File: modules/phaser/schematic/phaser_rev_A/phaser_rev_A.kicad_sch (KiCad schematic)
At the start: 15 parts, among them Q1 2N2978, Q2 2N2978, Q3 2N2978, Q4 2N2978, Q5 2N2978

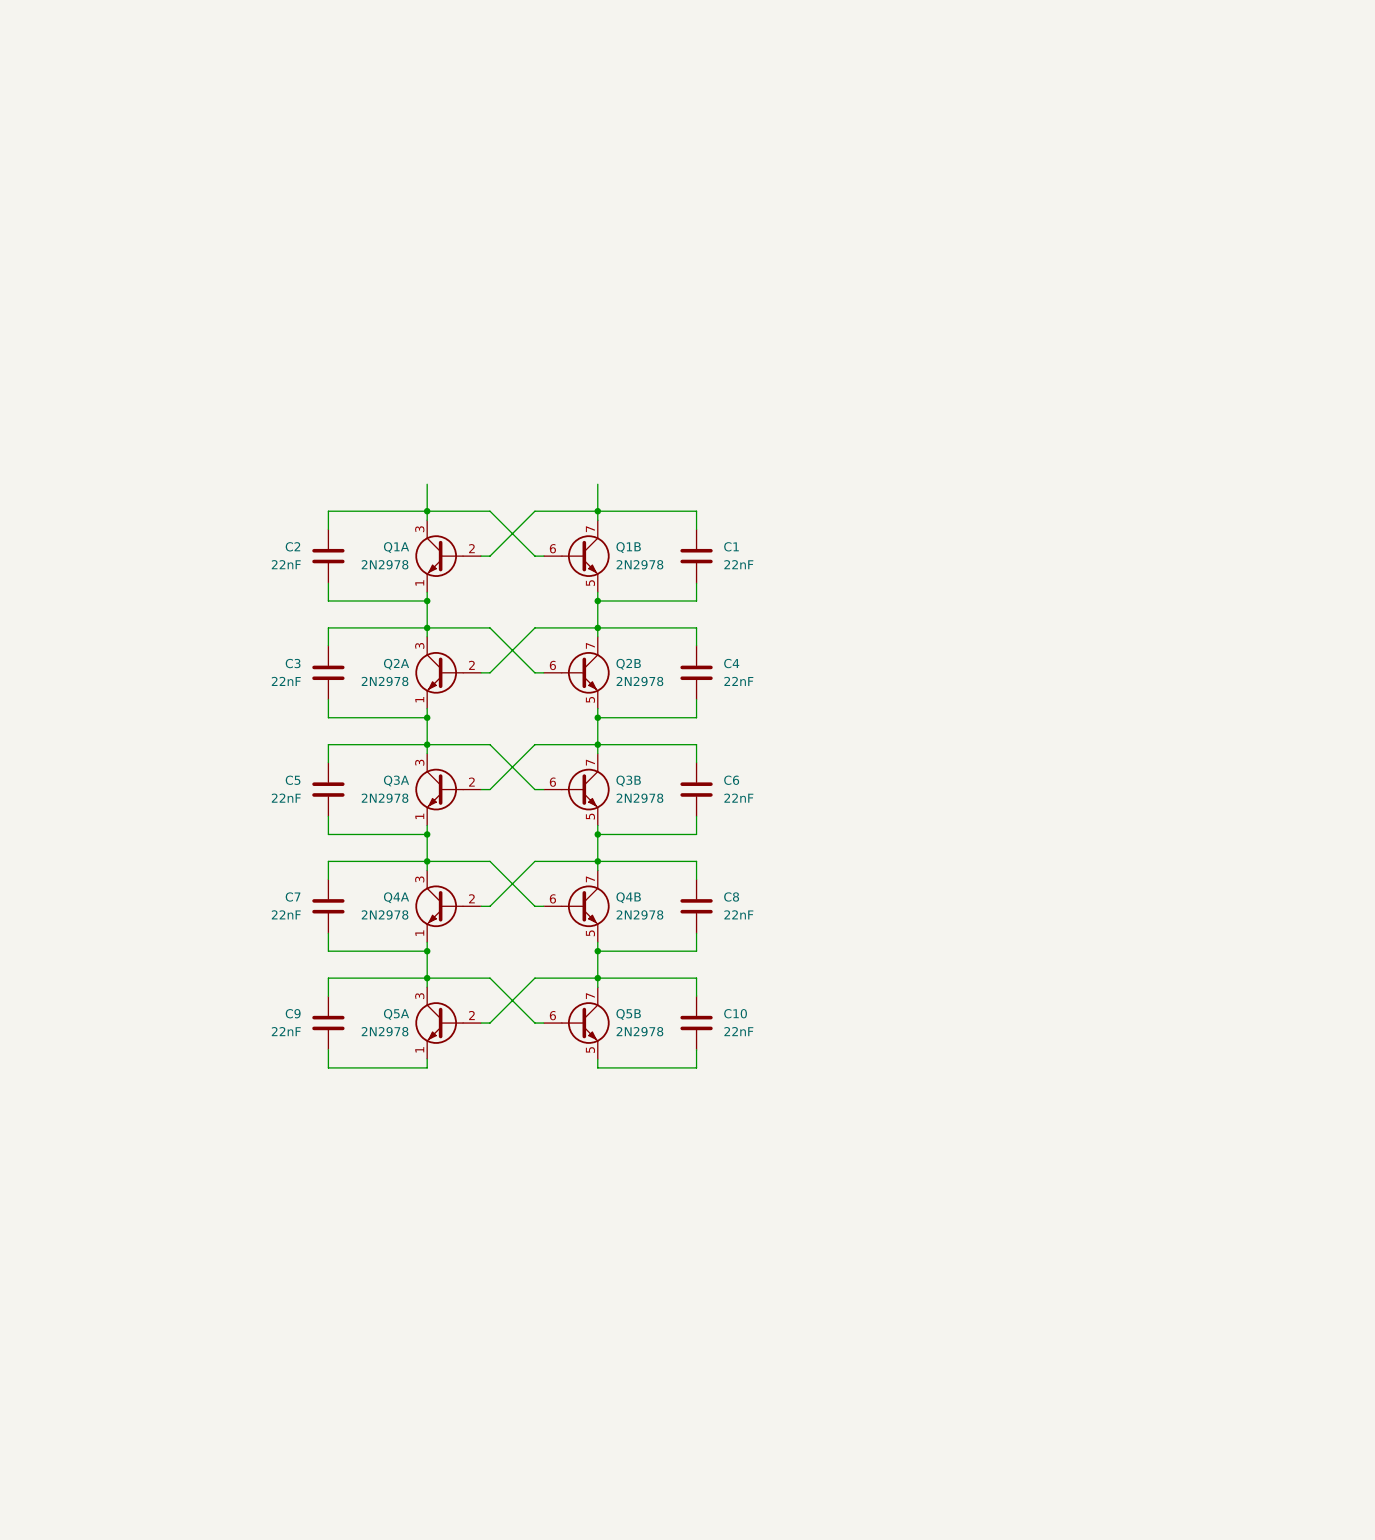
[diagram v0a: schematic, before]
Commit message: first routing of the PCB added a case study for the phaser
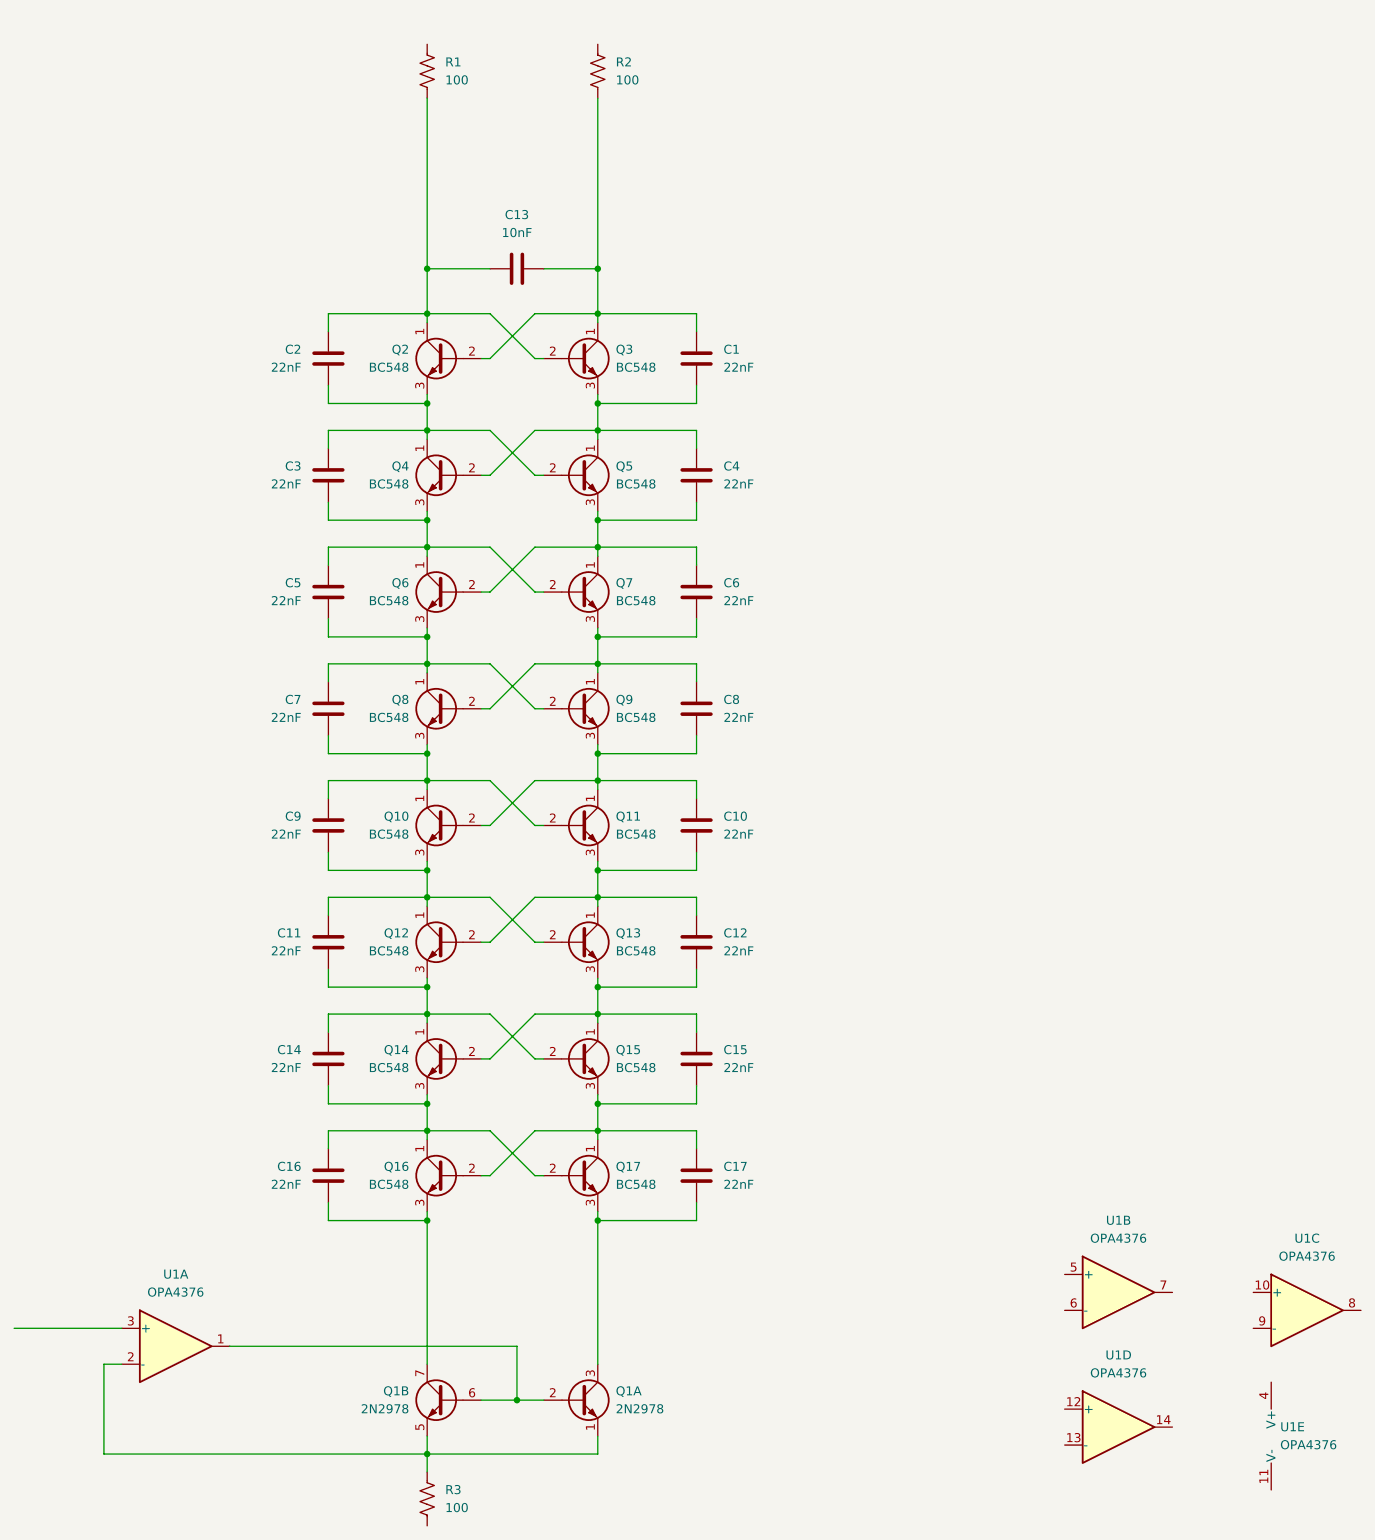
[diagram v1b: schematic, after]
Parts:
- removed Q2, Q3, Q4, Q5: 2N2978, ProjectLib_Transient:TO-5-6, symbol ProjectLib_Transient:2N2978
- added C11, C12, C14, C15, C16, C17: 22nF, Capacitor_THT:C_Rect_L7.0mm_W2.0mm_P5.00mm, symbol Device:C
- added C13: 10nF, Capacitor_THT:C_Rect_L7.0mm_W2.0mm_P5.00mm, symbol Device:C
- added Q10, Q11, Q12, Q13, Q14, Q15, Q16, Q17, Q2, Q3, Q4, Q5, Q6, Q7, Q8, Q9: BC548, Package_TO_SOT_THT:TO-92L_Inline_Wide, symbol Transistor_BJT:BC548
- added R1, R2, R3: 100, Resistor_THT:R_Axial_DIN0207_L6.3mm_D2.5mm_P10.16mm_Horizontal, symbol Device:R_US
- added U1: OPA4376, Package_DIP:DIP-14_W7.62mm_LongPads, symbol Amplifier_Operational:OPA4376
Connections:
- net at C9.2: now also C11.1, Q10.3 (E), Q12.1 (C), Q13.2 (B)
- net at C10.1, C8.2: now also Q10.2 (B), Q11.1 (C), Q9.3 (E)
- net at C7.2, C9.1: now also Q10.1 (C), Q11.2 (B), Q8.3 (E)
- net at C5.2, C7.1: now also Q6.3 (E), Q8.1 (C), Q9.2 (B)
- net at C6.2, C8.1: now also Q7.3 (E), Q8.2 (B), Q9.1 (C)
- net at C2.2, C3.1: now also Q2.3 (E), Q4.1 (C), Q5.2 (B); no longer Q1.1 (E1)
- net at C3.2, C5.1: now also Q4.3 (E), Q6.1 (C), Q7.2 (B)
- net at C1.2, C4.1: now also Q3.3 (E), Q4.2 (B), Q5.1 (C); no longer Q1.5 (E2)
- net at C10.2: now also C12.1, Q11.3 (E), Q12.2 (B), Q13.1 (C)
- net at C4.2, C6.1: now also Q5.3 (E), Q6.2 (B), Q7.1 (C)
- new net: C1.1, C13.2, Q2.2 (B), Q3.1 (C), R2.2
- new net: C13.1, C2.1, Q2.1 (C), Q3.2 (B), R1.2
- new net: C12.2, C15.1, Q13.3 (E), Q14.2 (B), Q15.1 (C)
- new net: C11.2, C14.1, Q12.3 (E), Q14.1 (C), Q15.2 (B)
- new net: C15.2, C17.1, Q15.3 (E), Q16.2 (B), Q17.1 (C)
- new net: C14.2, C16.1, Q14.3 (E), Q16.1 (C), Q17.2 (B)
- new net: C17.2, Q1.3 (C1), Q17.3 (E)
- new net: Q1.2 (B1), Q1.6 (B2), U1.1
- new net: Q1.1 (E1), Q1.5 (E2), R3.1, U1.2 (-)
- new net: C16.2, Q1.7 (C2), Q16.3 (E)
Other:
- moved on the sheet: C1, C10, C2, C3, C4, C5, C6, C7, C8, C9

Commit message: updated pcb layout
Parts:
- added C18, C19: 33µF, Capacitor_THT:CP_Radial_D8.0mm_P3.80mm, symbol Device:C_Polarized
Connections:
- net at C1.1, C13.2, Q2.2 (B)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: now also C18.1
- net at C13.1, C2.1, Q2.1 (C)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: now also C19.1
- net at R2.1: now also R1.1
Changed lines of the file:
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@@
 	)
 	(junction
+		(at 120.65 62.23)
+		(diameter 0)
+		(color 0 0 0 0)
+	)
+	(junction
 		(at 120.65 179.07)
 		(diameter 0)
@@
 	)
 	(junction
+		(at 144.78 38.1)
+		(diameter 0)
+		(color 0 0 0 0)
+	)
+	(junction
 		(at 120.65 158.75)
 		(diameter 0)
@@
 	)
 	(junction
+		(at 144.78 54.61)
+		(diameter 0)
+		(color 0 0 0 0)
+	)
+	(junction
 		(at 120.65 80.01)
 		(diameter 0)
@@
 	(wire
 		(pts
+			(xy 120.65 41.91) (xy 120.65 38.1)
+		)
+		(stroke
+			(width 0)
+			(type default)
+		)
+	)
+	(wire
+		(pts
 			(xy 120.65 195.58) (xy 120.65 196.85)
 		)
@@
 	(wire
 		(pts
+			(xy 144.78 54.61) (xy 144.78 73.66)
+		)
+		(stroke
+			(width 0)
+			(type default)
+		)
+	)
+	(wire
+		(pts
 			(xy 120.65 73.66) (xy 129.54 73.66)
 		)
@@
 	(wire
 		(pts
+			(xy 168.91 62.23) (xy 177.8 62.23)
+		)
+		(stroke
+			(width 0)
+			(type default)
+		)
+	)
+	(wire
+		(pts
 			(xy 120.65 80.01) (xy 129.54 80.01)
 		)
@@
 	(wire
 		(pts
+			(xy 120.65 62.23) (xy 120.65 73.66)
+		)
+		(stroke
+			(width 0)
+			(type default)
+		)
+	)
+	(wire
+		(pts
 			(xy 135.89 152.4) (xy 129.54 146.05)
 		)
@@
 	(wire
 		(pts
+			(xy 144.78 38.1) (xy 144.78 41.91)
+		)
+		(stroke
+			(width 0)
+			(type default)
+		)
+	)
+	(wire
+		(pts
 			(xy 158.75 82.55) (xy 158.75 80.01)
 		)
@@
 	(wire
 		(pts
+			(xy 120.65 62.23) (xy 161.29 62.23)
+		)
+		(stroke
+			(width 0)
+			(type default)
+		)
+	)
+	(wire
+		(pts
 			(xy 135.89 168.91) (xy 129.54 162.56)
 		)
@@
 	(wire
 		(pts
-			(xy 120.65 49.53) (xy 120.65 73.66)
+			(xy 120.65 49.53) (xy 120.65 62.23)
 		)
 		(stroke
@@
 	(wire
 		(pts
+			(xy 168.91 54.61) (xy 177.8 54.61)
+		)
+		(stroke
+			(width 0)
+			(type default)
+		)
+	)
+	(wire
+		(pts
 			(xy 144.78 173.99) (xy 144.78 175.26)
 		)
@@
 	(wire
 		(pts
-			(xy 144.78 49.53) (xy 144.78 73.66)
+			(xy 144.78 49.53) (xy 144.78 54.61)
 		)
 		(stroke
@@
 	(wire
 		(pts
+			(xy 144.78 54.61) (xy 161.29 54.61)
+		)
+		(stroke
+			(width 0)
+			(type default)
+		)
+	)
+	(wire
+		(pts
 			(xy 144.78 109.22) (xy 144.78 113.03)
 		)
@@
 	(wire
 		(pts
+			(xy 144.78 38.1) (xy 167.64 38.1)
+		)
+		(stroke
+			(width 0)
+			(type default)
+		)
+	)
+	(wire
+		(pts
+			(xy 120.65 38.1) (xy 144.78 38.1)
+		)
+		(stroke
+			(width 0)
+			(type default)
+		)
+	)
+	(wire
+		(pts
 			(xy 144.78 125.73) (xy 144.78 129.54)
 		)
@@
 	)
 	(symbol
+		(lib_id "Device:C_Polarized")
+		(at 165.1 54.61 90)
+		(unit 1)
+		(exclude_from_sim no)
+		(in_bom yes)
+		(on_board yes)
+		(dnp no)
+		(fields_autoplaced yes)
+		(property "Reference" "C18"
+			(at 164.211 46.99 90)
+			(effects
+				(font
+					(size 1.27 1.27)
+				)
+			)
+		)
+		(property "Value" "33µF"
+			(at 164.211 49.53 90)
+			(effects
+				(font
+					(size 1.27 1.27)
+				)
+			)
+		)
+		(property "Footprint" "Capacitor_THT:CP_Radial_D8.0mm_P3.80mm"
+			(at 168.91 53.6448 0)
+			(effects
+				(font
+					(size 1.27 1.27)
+				)
+				(hide yes)
+			)
+		)
+		(property "Datasheet" "~"
+			(at 165.1 54.61 0)
+			(effects
+				(font
+					(size 1.27 1.27)
+				)
+				(hide yes)
+			)
+		)
+		(property "Description" "Polarized capacitor"
+			(at 165.1 54.61 0)
+			(effects
+				(font
+					(size 1.27 1.27)
+				)
+				(hide yes)
+			)
+		)
+		(pin "2"
+		)
+		(pin "1"
+		)
+		(instances
+			(project ""
+				(path "/197f4a44-5606-4614-9f30-04e68d42fe94"
+					(reference "C18")
+					(unit 1)
+				)
+			)
+		)
+	)
+	(symbol
 		(lib_id "Transistor_BJT:BC548")
 		(at 142.24 135.89 0)
@@
 					(unit 1)
 				)
+			)
+		)
+	)
+	(symbol
+		(lib_id "Device:C_Polarized")
+		(at 165.1 62.23 90)
+		(mirror x)
+		(unit 1)
+		(exclude_from_sim no)
+		(in_bom yes)
+		(on_board yes)
+		(dnp no)
+		(property "Reference" "C19"
+			(at 164.211 69.85 90)
+			(effects
+				(font
+					(size 1.27 1.27)
+				)
+			)
+		)
+		(property "Value" "33µF"
+			(at 164.211 67.31 90)
+			(effects
+				(font
+					(size 1.27 1.27)
+				)
+			)
+		)
+		(property "Footprint" "Capacitor_THT:CP_Radial_D8.0mm_P3.80mm"
+			(at 168.91 63.1952 0)
+			(effects
+				(font
+					(size 1.27 1.27)
+				)
+				(hide yes)
+			)
+		)
+		(property "Datasheet" "~"
+			(at 165.1 62.23 0)
+			(effects
+				(font
+					(size 1.27 1.27)
+				)
+				(hide yes)
+			)
+		)
+		(property "Description" "Polarized capacitor"
+			(at 165.1 62.23 0)
+			(effects
+				(font
+					(size 1.27 1.27)
+				)
+				(hide yes)
+			)
+		)
+		(pin "2"
+		)
+		(pin "1"
+		)
+		(instances
+			(project "phaser_rev_A"
+				(path "/197f4a44-5606-4614-9f30-04e68d42fe94"
+					(reference "C19")
+					(unit 1)
+				)
